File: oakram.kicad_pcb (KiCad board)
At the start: 2 copper layers, 42.5 x 54 mm, 20 parts, among them U1 IS41C16105C, U2 IS41C16105C, X1 ZIP40, X2 ZIP40

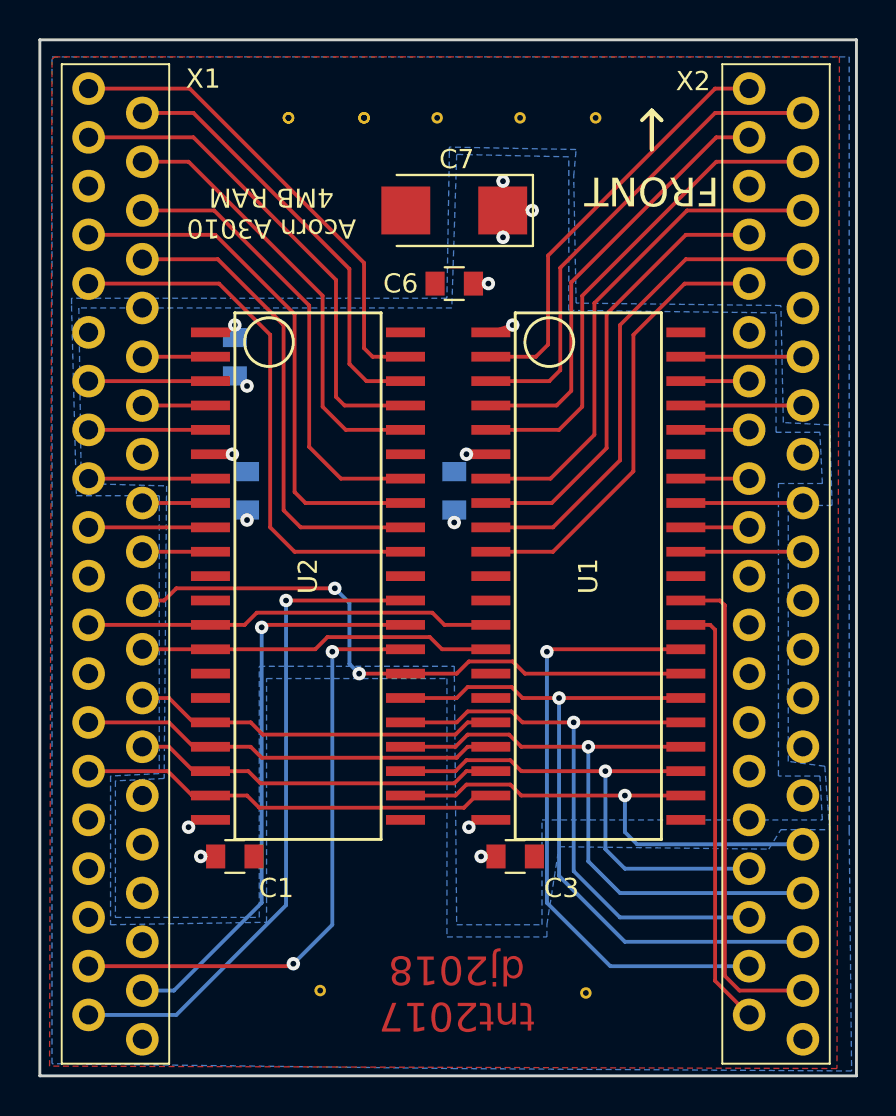
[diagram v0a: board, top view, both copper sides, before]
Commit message: oakramv3 from https://stardot.org.uk/forums/viewtopic.php?f=16&t=11214&p=237523#p201999
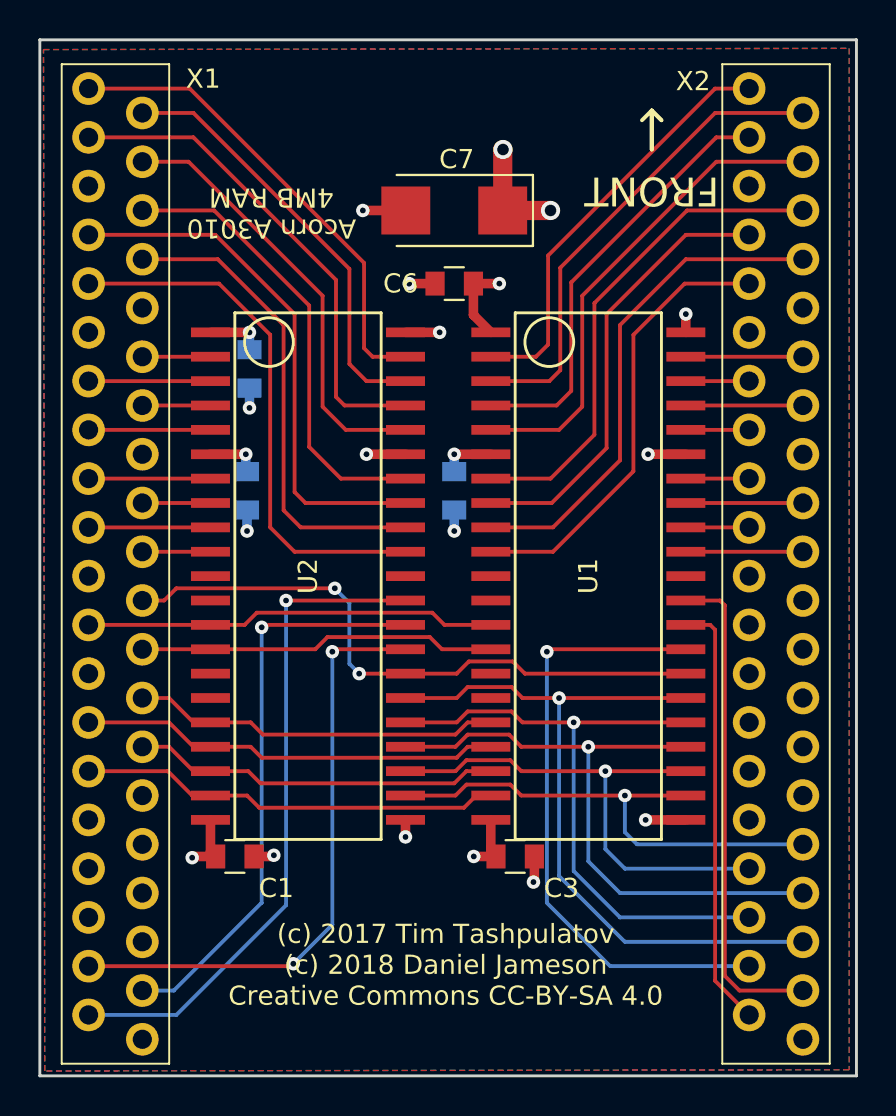
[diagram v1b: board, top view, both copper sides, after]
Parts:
- removed ? (x9): VIA-0.6mm, VIA-0.6mm
- moved C5 0.99 mm to (130.3, 90.8)
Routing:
- net VSS: track 2.17 -> 18.9 mm, vias 3 -> 13
- net VCC: track 15.5 -> 27.3 mm, vias 12 -> 8
- added copper zone on In2.Cu, net VCC
- added copper zone on In1.Cu, net VSS
- removed copper zone on B.Cu, net VCC
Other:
- copper layers 2 -> 4
- board text added: "(c) 2017 Tim Tashpulatov (c) 2018 Daniel Jameson Creative Commons CC-BY-SA 4.0"
- board text removed: "tnt2017 dj2018"

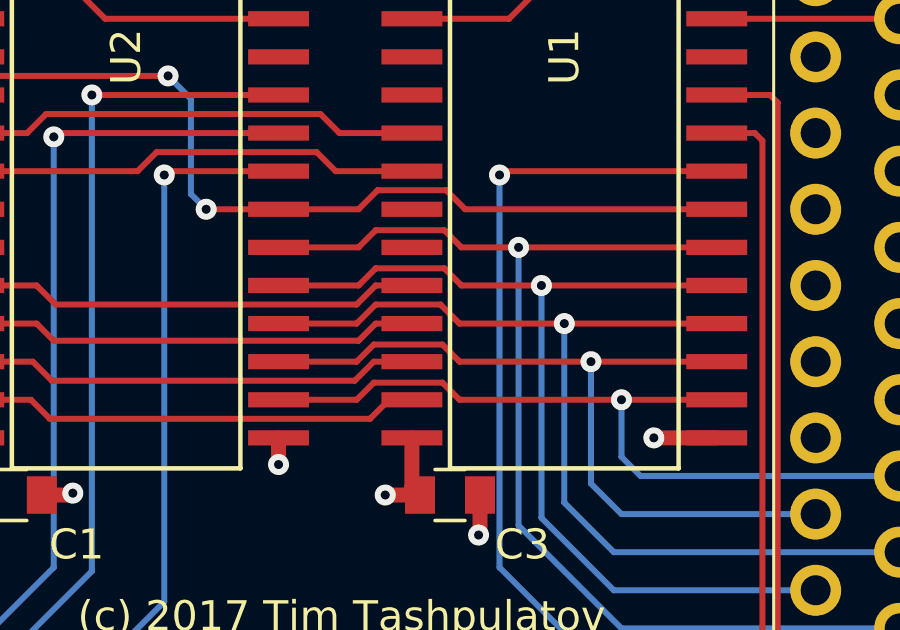
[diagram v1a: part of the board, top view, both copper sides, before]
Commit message: Added 7mil clearance and changed min width on all pours to 7mil, then fixed DRC
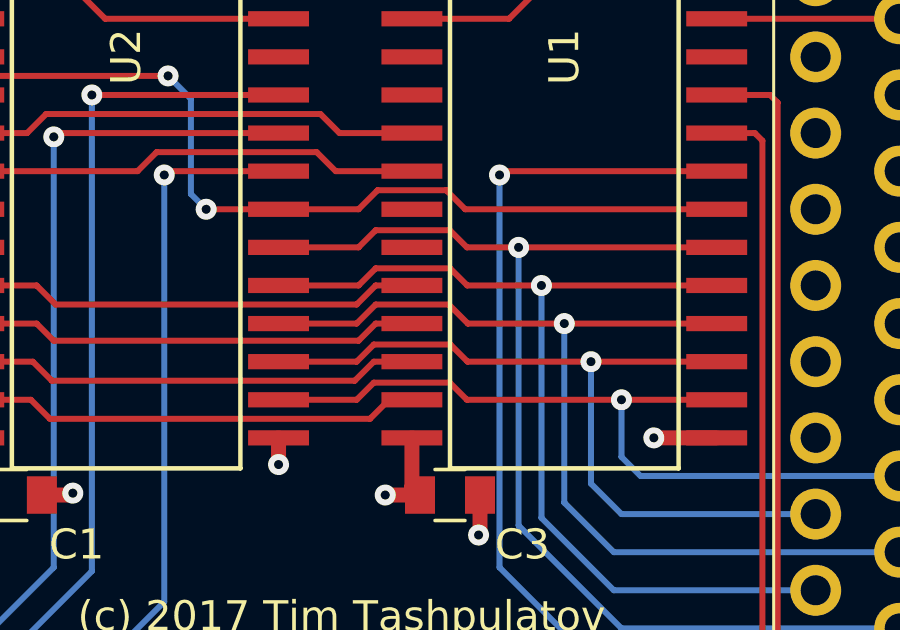
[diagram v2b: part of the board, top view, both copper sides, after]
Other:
- net class Default: clearance 0 -> 0.1778
- rule trace_clearance: 0 -> 0.1778
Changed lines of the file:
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@@
-(kicad_pcb (version 4) (host pcbnew 4.0.7)
+(kicad_pcb (version 20171130) (host pcbnew "(5.0.1-3-g963ef8bb5)")
   (general
-    (links 99)
-    (no_connects 1)
-    (area 119.304999 73.584999 178.665 136.050001)
     (thickness 1.6)
     (drawings 16)
@@
   )
   (layers
-    (0 F.Cu signal hide)
-    (1 In1.Cu power hide)
-    (2 In2.Cu power hide)
-    (31 B.Cu signal hide)
+    (0 F.Cu signal)
+    (1 In1.Cu power)
+    (2 In2.Cu power)
+    (31 B.Cu signal)
     (32 B.Adhes user)
     (33 F.Adhes user)
@@
     (user_trace_width 0.8)
     (user_trace_width 1)
-    (trace_clearance 0)
+    (trace_clearance 0.1778)
     (zone_clearance 0.254)
     (zone_45_only no)
@@
     (pad_drill 0.3)
     (pad_to_mask_clearance 0.2)
+    (solder_mask_min_width 0.25)
     (aux_axis_origin 0 0)
     (visible_elements 7FFFFFFF)
@@
       (usegerberextensions false)
       (usegerberattributes true)
+      (usegerberadvancedattributes false)
+      (creategerberjobfile false)
       (excludeedgelayer true)
       (linewidth 0.100000)
@@
       (hpglpennumber 1)
       (hpglpenspeed 20)
-      (hpglpendiameter 15)
-      (hpglpenoverlay 2)
+      (hpglpendiameter 15.000000)
       (psnegative false)
       (psa4output false)
@@
       (drillshape 0)
       (scaleselection 1)
-      (outputdirectory gerbers))
+      (outputdirectory "gerbers"))
   )
   (net 0 "")
@@
   (net 73 "Net-(X2-Pad27)")
   (net_class Default "This is the default net class."
-    (clearance 0)
+    (clearance 0.1778)
     (trace_width 0.25)
     (via_dia 0.7)
@@
     (tags "capacitor tantalum smd")
     (attr smd)
-    (fp_text reference C7 (at -0.127 2.667 360) (layer F.SilkS)
+    (fp_text reference C7 (at -0.127 2.667) (layer F.SilkS)
       (effects (font (size 1 1) (thickness 0.15)))
     )
@@
   (segment (start 149.86 114.935) (end 150.495 115.57) (width 0.2) (layer B.Cu) (net 20))
   (segment (start 149.86 114.935) (end 149.86 113.03) (width 0.2) (layer B.Cu) (net 20))
-  (segment (start 138.43 113.03) (end 141.0335 113.03) (width 0.2) (layer F.Cu) (net 20) (status 10))
-  (segment (start 144.4625 113.03) (end 149.86 113.03) (width 0.2) (layer F.Cu) (net 20))
   (segment (start 149.86 113.03) (end 153.035 113.03) (width 0.2) (layer F.Cu) (net 20) (status 20))
-  (segment (start 143.891 112.4585) (end 144.4625 113.03) (width 0.2) (layer F.Cu) (net 20))
-  (segment (start 141.605 112.4585) (end 143.891 112.4585) (width 0.2) (layer F.Cu) (net 20))
+  (segment (start 144.71 113.03) (end 149.86 113.03) (width 0.2) (layer F.Cu) (net 20))
+  (segment (start 144.1385 112.4585) (end 144.71 113.03) (width 0.2) (layer F.Cu) (net 20))
+  (segment (start 141.605 112.4585) (end 144.1385 112.4585) (width 0.2) (layer F.Cu) (net 20))
   (segment (start 141.0335 113.03) (end 141.605 112.4585) (width 0.2) (layer F.Cu) (net 20))
+  (segment (start 138.43 113.03) (end 141.0335 113.03) (width 0.2) (layer F.Cu) (net 20))
   (segment (start 128.27 97.79) (end 124.72 97.79) (width 0.2) (layer F.Cu) (net 21) (status 30))
   (segment (start 128.27 100.33) (end 124.72 100.33) (width 0.2) (layer F.Cu) (net 22) (status 30))
@@
   (segment (start 147.955 116.459) (end 147.955 110.49) (width 0.2) (layer B.Cu) (net 28))
   (segment (start 153.035 110.49) (end 147.955 110.49) (width 0.2) (layer F.Cu) (net 28) (status 10))
-  (segment (start 147.955 110.49) (end 144.4625 110.49) (width 0.2) (layer F.Cu) (net 28))
+  (segment (start 144.105 109.855) (end 144.74 110.49) (width 0.2) (layer F.Cu) (net 28))
+  (segment (start 144.74 110.49) (end 147.955 110.49) (width 0.2) (layer F.Cu) (net 28))
+  (segment (start 141.6685 109.855) (end 144.105 109.855) (width 0.2) (layer F.Cu) (net 28))
   (segment (start 141.0335 110.49) (end 141.6685 109.855) (width 0.2) (layer F.Cu) (net 28))
-  (segment (start 141.6685 109.855) (end 143.8275 109.855) (width 0.2) (layer F.Cu) (net 28))
-  (segment (start 143.8275 109.855) (end 144.4625 110.49) (width 0.2) (layer F.Cu) (net 28))
-  (segment (start 141.0335 110.49) (end 138.43 110.49) (width 0.2) (layer F.Cu) (net 28) (status 20))
+  (segment (start 138.43 110.49) (end 141.0335 110.49) (width 0.2) (layer F.Cu) (net 28))
   (segment (start 146.431 107.95) (end 146.431 117.221) (width 0.2) (layer B.Cu) (net 29))
   (via (at 146.431 107.95) (size 0.7) (drill 0.3) (layers F.Cu B.Cu) (net 29))
   (segment (start 149.86 120.65) (end 159.134 120.65) (width 0.2) (layer B.Cu) (net 29) (status 20))
   (segment (start 146.431 117.221) (end 149.86 120.65) (width 0.2) (layer B.Cu) (net 29))
-  (segment (start 138.43 107.95) (end 141.097 107.95) (width 0.2) (layer F.Cu) (net 29) (status 10))
-  (segment (start 144.526 107.95) (end 146.431 107.95) (width 0.2) (layer F.Cu) (net 29))
   (segment (start 146.431 107.95) (end 153.035 107.95) (width 0.2) (layer F.Cu) (net 29) (status 20))
-  (segment (start 143.9545 107.3785) (end 144.526 107.95) (width 0.2) (layer F.Cu) (net 29))
-  (segment (start 141.6685 107.3785) (end 143.9545 107.3785) (width 0.2) (layer F.Cu) (net 29))
+  (segment (start 144.1385 107.3785) (end 144.71 107.95) (width 0.2) (layer F.Cu) (net 29))
+  (segment (start 141.6685 107.3785) (end 144.1385 107.3785) (width 0.2) (layer F.Cu) (net 29))
+  (segment (start 144.71 107.95) (end 146.431 107.95) (width 0.2) (layer F.Cu) (net 29))
   (segment (start 141.097 107.95) (end 141.6685 107.3785) (width 0.2) (layer F.Cu) (net 29))
+  (segment (start 138.43 107.95) (end 141.097 107.95) (width 0.2) (layer F.Cu) (net 29))
   (segment (start 121.92 124.46) (end 126.492 124.46) (width 0.2) (layer B.Cu) (net 30) (status 10))
   (segment (start 132.207 118.745) (end 132.207 102.87) (width 0.2) (layer B.Cu) (net 30))
@@
   (segment (start 149.606 119.38) (end 156.334 119.38) (width 0.2) (layer B.Cu) (net 32) (status 20))
   (segment (start 147.193 116.967) (end 149.606 119.38) (width 0.2) (layer B.Cu) (net 32))
-  (segment (start 138.43 109.22) (end 141.097 109.22) (width 0.2) (layer F.Cu) (net 32) (status 10))
-  (segment (start 144.526 109.22) (end 147.193 109.22) (width 0.2) (layer F.Cu) (net 32))
   (segment (start 147.193 109.22) (end 153.035 109.22) (width 0.2) (layer F.Cu) (net 32) (status 20))
-  (segment (start 143.9545 108.6485) (end 144.526 109.22) (width 0.2) (layer F.Cu) (net 32))
-  (segment (start 141.6685 108.6485) (end 143.9545 108.6485) (width 0.2) (layer F.Cu) (net 32))
+  (segment (start 144.72 109.22) (end 147.193 109.22) (width 0.2) (layer F.Cu) (net 32))
+  (segment (start 144.1485 108.6485) (end 144.72 109.22) (width 0.2) (layer F.Cu) (net 32))
+  (segment (start 141.6685 108.6485) (end 144.1485 108.6485) (width 0.2) (layer F.Cu) (net 32))
   (segment (start 141.097 109.22) (end 141.6685 108.6485) (width 0.2) (layer F.Cu) (net 32))
+  (segment (start 138.43 109.22) (end 141.097 109.22) (width 0.2) (layer F.Cu) (net 32))
   (via (at 148.844 111.76) (size 0.7) (drill 0.3) (layers F.Cu B.Cu) (net 33))
   (segment (start 156.334 116.84) (end 149.86 116.84) (width 0.2) (layer B.Cu) (net 33) (status 10))
   (segment (start 148.844 115.824) (end 149.86 116.84) (width 0.2) (layer B.Cu) (net 33))
   (segment (start 148.844 115.824) (end 148.844 111.76) (width 0.2) (layer B.Cu) (net 33))
-  (segment (start 138.43 111.76) (end 141.0335 111.76) (width 0.2) (layer F.Cu) (net 33) (status 10))
-  (segment (start 144.4625 111.76) (end 148.844 111.76) (width 0.2) (layer F.Cu) (net 33))
   (segment (start 148.844 111.76) (end 153.035 111.76) (width 0.2) (layer F.Cu) (net 33) (status 20))
-  (segment (start 143.891 111.1885) (end 144.4625 111.76) (width 0.2) (layer F.Cu) (net 33))
-  (segment (start 141.605 111.1885) (end 143.891 111.1885) (width 0.2) (layer F.Cu) (net 33))
+  (segment (start 141.605 111.1885) (end 144.1585 111.1885) (width 0.2) (layer F.Cu) (net 33))
+  (segment (start 144.1585 111.1885) (end 144.73 111.76) (width 0.2) (layer F.Cu) (net 33))
   (segment (start 141.0335 111.76) (end 141.605 111.1885) (width 0.2) (layer F.Cu) (net 33))
+  (segment (start 144.73 111.76) (end 148.844 111.76) (width 0.2) (layer F.Cu) (net 33))
+  (segment (start 138.43 111.76) (end 141.0335 111.76) (width 0.2) (layer F.Cu) (net 33))
   (segment (start 130.937 104.267) (end 130.937 118.618) (width 0.2) (layer B.Cu) (net 34))
   (segment (start 131.064 104.14) (end 130.937 104.267) (width 0.2) (layer F.Cu) (net 34))
@@
   (zone (net 56) (net_name VSS) (layer In1.Cu) (hatch edge 0.508)
     (connect_pads (clearance 0.254))
-    (min_thickness 0.0254)
+    (min_thickness 0.1778)
     (fill yes (arc_segments 16) (thermal_gap 0.508) (thermal_bridge_width 0.508))
     (polygon
@@
   (zone (net 57) (net_name VCC) (layer In2.Cu) (hatch edge 0.508)
     (connect_pads (clearance 0.254))
-    (min_thickness 0.0254)
+    (min_thickness 0.1778)
     (fill yes (arc_segments 16) (thermal_gap 0.508) (thermal_bridge_width 0.508))
     (polygon
@@
   (zone (net 57) (net_name VCC) (layer In2.Cu) (hatch edge 0.508)
     (connect_pads (clearance 0.254))
-    (min_thickness 0.0254)
+    (min_thickness 0.1778)
     (fill yes (arc_segments 16) (thermal_gap 0.508) (thermal_bridge_width 0.508))
     (polygon
@@
   (zone (net 56) (net_name VSS) (layer F.Cu) (hatch edge 0.508)
     (connect_pads (clearance 0.254))
-    (min_thickness 0.0254)
+    (min_thickness 0.1778)
     (fill yes (arc_segments 16) (thermal_gap 0.508) (thermal_bridge_width 0.508))
     (polygon
@@
   (zone (net 56) (net_name VSS) (layer B.Cu) (hatch edge 0.508)
     (connect_pads (clearance 0.254))
-    (min_thickness 0.0254)
+    (min_thickness 0.1778)
     (fill yes (arc_segments 16) (thermal_gap 0.508) (thermal_bridge_width 0.508))
     (polygon
